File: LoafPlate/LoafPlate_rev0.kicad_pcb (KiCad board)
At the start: 2 copper layers, 195.1 x 84 mm, 1 part

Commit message: Minor power revisions
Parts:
- removed REF**: Breadboard_Bus_2_Terminal_1_Ties_830, CustomFootprintLibrary:Breadboard_Busx02_Terminalx01_Tiesx830_WithMounts
- added C1: 1p, Capacitor_SMD:CP_Elec_3x5.3, F.Cu at (106.7, 60.3)
- added C2: 100n, Capacitor_SMD:C_0603_1608Metric, F.Cu at (241.4, 74.7)
- added C3: 100n, Capacitor_SMD:C_0603_1608Metric, F.Cu at (241.4, 112.1)
- added C4: 1p, Capacitor_SMD:CP_Elec_3x5.3, F.Cu at (106.7, 66.7)
- added C5: 100n, Capacitor_SMD:C_0603_1608Metric, F.Cu at (235.1, 113.8)
- added C6: 100n, Capacitor_SMD:C_0603_1608Metric, F.Cu at (236.1, 77.2)
- added D1: +5V_PWR, LED_SMD:LED_1206_3216Metric, F.Cu at (188.0, 66.5)
- added D2: +3V3_PWR, LED_SMD:LED_1206_3216Metric, F.Cu at (196.8, 66.5)
- added J1: Ext Connector, Connector_IDC:IDC-Header_2x05_P2.54mm_Horizontal, F.Cu at (85.1, 67.3)
- added J2: Rail Power, Connector_PinSocket_2.54mm:PinSocket_1x04_P2.54mm_Vertical, F.Cu at (238.8, 75.6)
- added J3: Rail Power, Connector_PinSocket_2.54mm:PinSocket_1x04_P2.54mm_Vertical, F.Cu at (238.8, 113.0)
- added PLT1: BasePlate, CustomFootprintLibrary:Breadboard_Busx02_Terminalx01_Tiesx830_WithMounts, F.Cu at (149.9, 97.8)
- added R1: 120, Resistor_SMD:R_1206_3216Metric, F.Cu at (185.5, 63.6)
- added R2: 15, Resistor_SMD:R_1206_3216Metric, F.Cu at (194.4, 63.6)
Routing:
- net VCC: track 0.00 -> 236.7 mm
- net +3.3V: track 0.00 -> 217.0 mm, vias 0 -> 2
- net +5V: track 0.00 -> 215.0 mm
- net GND: track 0.00 -> 16.7 mm, vias 0 -> 10
- net Net-(D1-Pad1): track 0.00 -> 2.44 mm
- net Net-(D2-Pad1): track 0.00 -> 2.44 mm
- added copper zone on B.Cu, net GND
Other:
- rule pad_to_mask_clearance: 0 -> 0.05

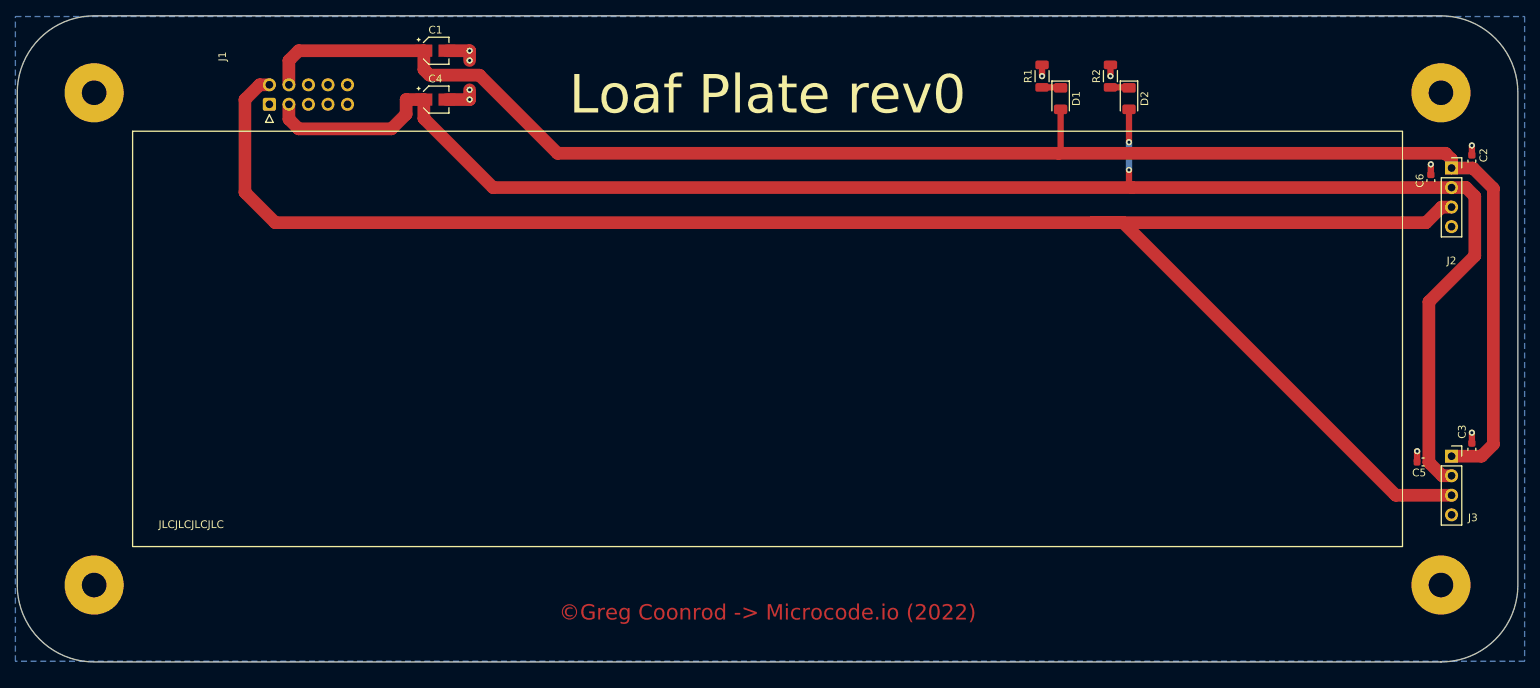
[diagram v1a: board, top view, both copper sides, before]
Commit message: Redo layout and routing
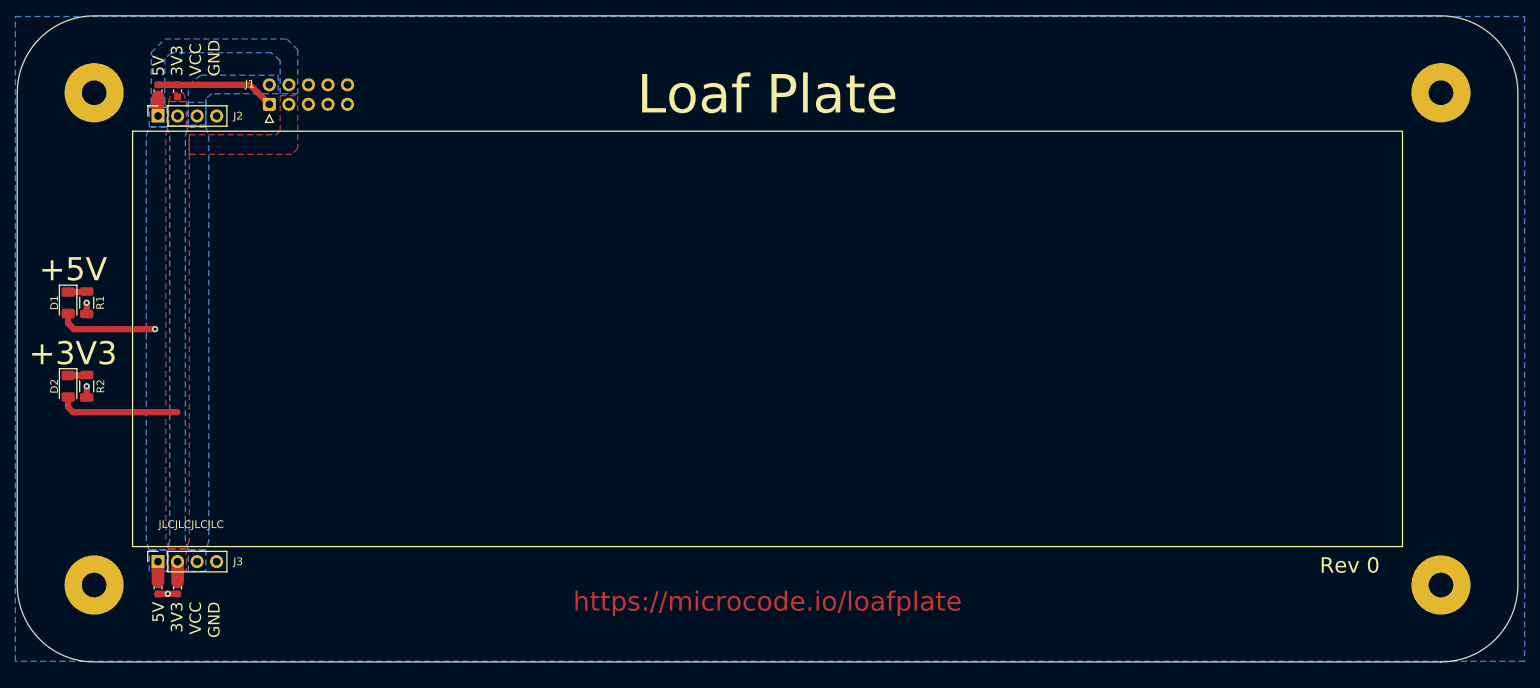
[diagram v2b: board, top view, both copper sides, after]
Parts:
- removed the C1 at (106.7, 60.3)
- removed the C4 at (106.7, 66.7)
- moved C2 171.8 mm to (70.6, 130.2), turned to -90 degrees
- moved C1 171.1 mm to (70.6, 65.5)
- moved J3 168.7 mm to (70.6, 126.7), turned to 90 degrees
- moved J2 168.3 mm to (70.6, 68.8), turned to 90 degrees
- moved C4 163.4 mm to (73.2, 65.5)
- moved C3 162.8 mm to (73.2, 130.2), turned to -90 degrees
- moved D2 142.9 mm to (58.9, 103.9)
- moved R2 139.1 mm to (61.3, 103.9), turned to -90 degrees
- moved D1 131.7 mm to (58.9, 93.1)
- moved R1 127.7 mm to (61.3, 93.1), turned to -90 degrees
- renumbered C2 to C1, C3 to C2, C5 to C3, C6 to C4
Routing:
- net VCC: track 236.7 -> 0.00 mm
- net +3.3V: track 217.0 -> 18.5 mm, vias 2 -> 0
- net +5V: track 215.0 -> 18.0 mm, vias 0 -> 1
- net GND: track 16.7 -> 21.0 mm, vias 10 -> 3
- added copper zone on F.Cu, net +3.3V
- added copper zone on B.Cu, net +5V
- added copper zone on B.Cu, net VCC
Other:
- board text added: "+3V3"
- board text added: "+5V"
- board text added: "5V 3V3 VCC GND"
- board text added: "Loaf Plate"
- board text added: "Rev 0"
- board text added: "https://microcode.io/loafplate"
- board text removed: "Loaf Plate rev0"
- board text removed: "©Greg Coonrod -> Microcode.io (2022)"

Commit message: Added tooling holes for production.
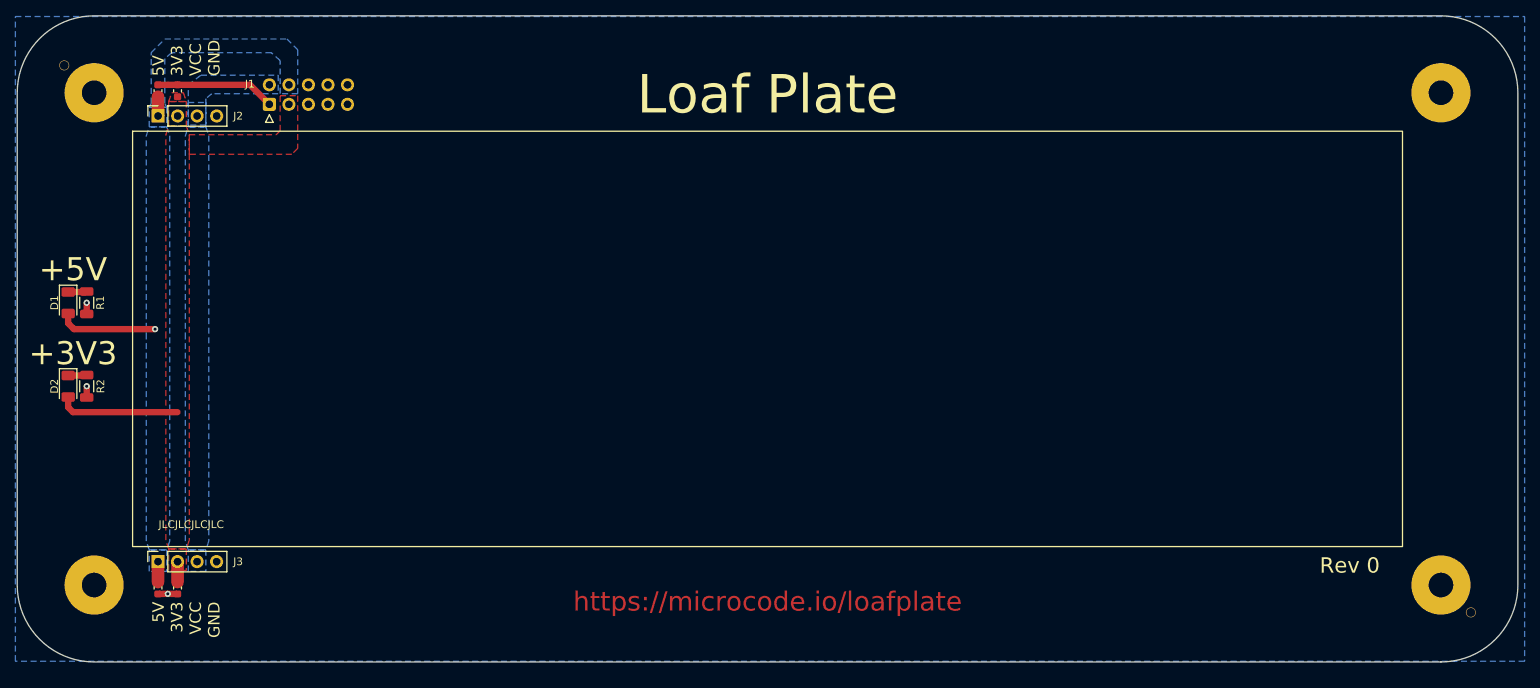
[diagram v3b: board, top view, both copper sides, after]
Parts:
- added H1: AssemblyToolingHole, ExtraParts:JLCPCB_ToolingHole, F.Cu at (58.4, 62.2)
- added H2: AssemblyToolingHole, ExtraParts:JLCPCB_ToolingHole, F.Cu at (241.3, 133.3)
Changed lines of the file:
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@@
     (property "Sheetfile" "LoafPlate_rev0.kicad_sch")
     (property "Sheetname" "")
+    (attr exclude_from_pos_files)
     (fp_text reference "PLT1" (at 0 0 unlocked) (layer "F.SilkS") hide
       (effects (font (size 1 1) (thickness 0.15)))
@@
     )
   )
+  (footprint "ExtraParts:JLCPCB_ToolingHole" (layer "F.Cu")
+    (at 58.42 62.23)
+    (descr "Mounting Hole 2.1mm, no annular")
+    (tags "mounting hole 2.1mm no annular")
+    (property "Sheetfile" "LoafPlate_rev0.kicad_sch")
+    (property "Sheetname" "")
+    (attr exclude_from_pos_files exclude_from_bom)
+    (fp_text reference "H1" (at 0 -2.54) (layer "F.SilkS") hide
+      (effects (font (size 1 1) (thickness 0.15)))
+    )
+    (fp_text value "AssemblyToolingHole" (at 0 2.54) (layer "F.Fab") hide
+      (effects (font (size 1 1) (thickness 0.15)))
+    )
+    (fp_text user "${REFERENCE}" (at -2.032 0) (layer "F.Fab")
+      (effects (font (size 1 1) (thickness 0.15)))
+    )
+    (fp_circle (center 0 0) (end 0.92 0) (layer "F.CrtYd") (width 0.05) (fill none))
+    (pad "" np_thru_hole circle (at 0 0) (size 1.3 1.3) (drill 1.152) (layers F&B.Cu *.Mask))
+  )
   (footprint "Capacitor_SMD:C_0603_1608Metric" (layer "F.Cu")
     (at 70.612 130.175 -90)
@@
       (rotate (xyz 0 0 0))
     )
+  )
+  (footprint "ExtraParts:JLCPCB_ToolingHole" (layer "F.Cu")
+    (at 241.3 133.35)
+    (descr "Mounting Hole 2.1mm, no annular")
+    (tags "mounting hole 2.1mm no annular")
+    (property "Sheetfile" "LoafPlate_rev0.kicad_sch")
+    (property "Sheetname" "")
+    (attr exclude_from_pos_files exclude_from_bom)
+    (fp_text reference "H2" (at 0 -2.54) (layer "F.SilkS") hide
+      (effects (font (size 1 1) (thickness 0.15)))
+    )
+    (fp_text value "AssemblyToolingHole" (at 0 2.54) (layer "F.Fab") hide
+      (effects (font (size 1 1) (thickness 0.15)))
+    )
+    (fp_text user "${REFERENCE}" (at 2.032 0) (layer "F.Fab")
+      (effects (font (size 1 1) (thickness 0.15)))
+    )
+    (fp_circle (center 0 0) (end 0.92 0) (layer "F.CrtYd") (width 0.05) (fill none))
+    (pad "" np_thru_hole circle (at 0 0) (size 1.3 1.3) (drill 1.152) (layers F&B.Cu *.Mask))
   )
   (footprint "Connector_PinSocket_2.54mm:PinSocket_1x04_P2.54mm_Vertical" (layer "F.Cu")
@@
     (min_thickness 0.254)
     (keepout (tracks allowed) (vias allowed) (pads not_allowed) (copperpour allowed) (footprints not_allowed))
-    (fill (thermal_gap 0.508) (thermal_bridge_width 0.508) (smoothing chamfer) (radius 0.25))
+    (fill (thermal_gap 0.508) (thermal_bridge_width 0.508))
     (polygon
       (pts
